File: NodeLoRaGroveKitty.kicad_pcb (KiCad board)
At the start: 2 copper layers, 37 parts, among them P1 PICKIT PROGRAMMER, P2 Battery, P3 A0, P4 D9, P5 USB-Serial, P6 I2C, SW1 SW_PUSH, SW2 SW_PUSH, U1 AP2112, U2 MCP73831T-2ATI/OT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

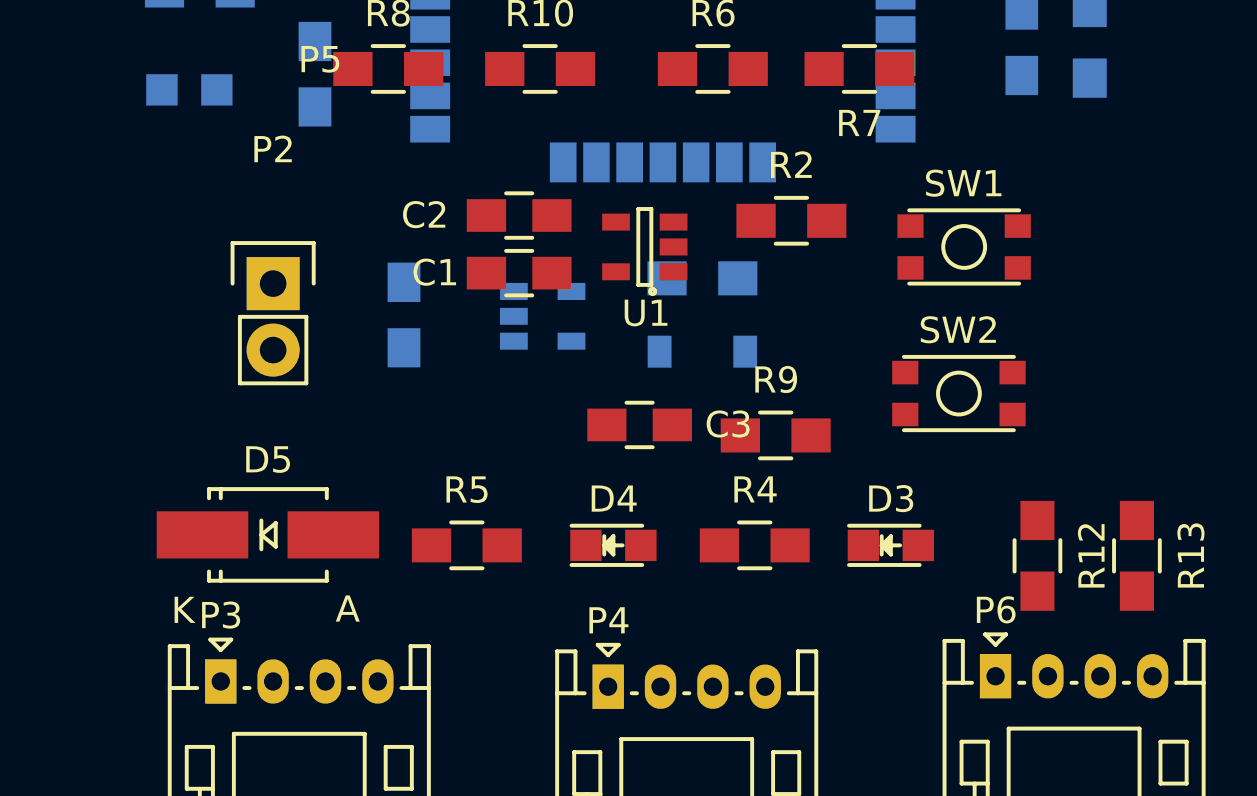
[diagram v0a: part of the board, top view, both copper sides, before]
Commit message: Validate footprints
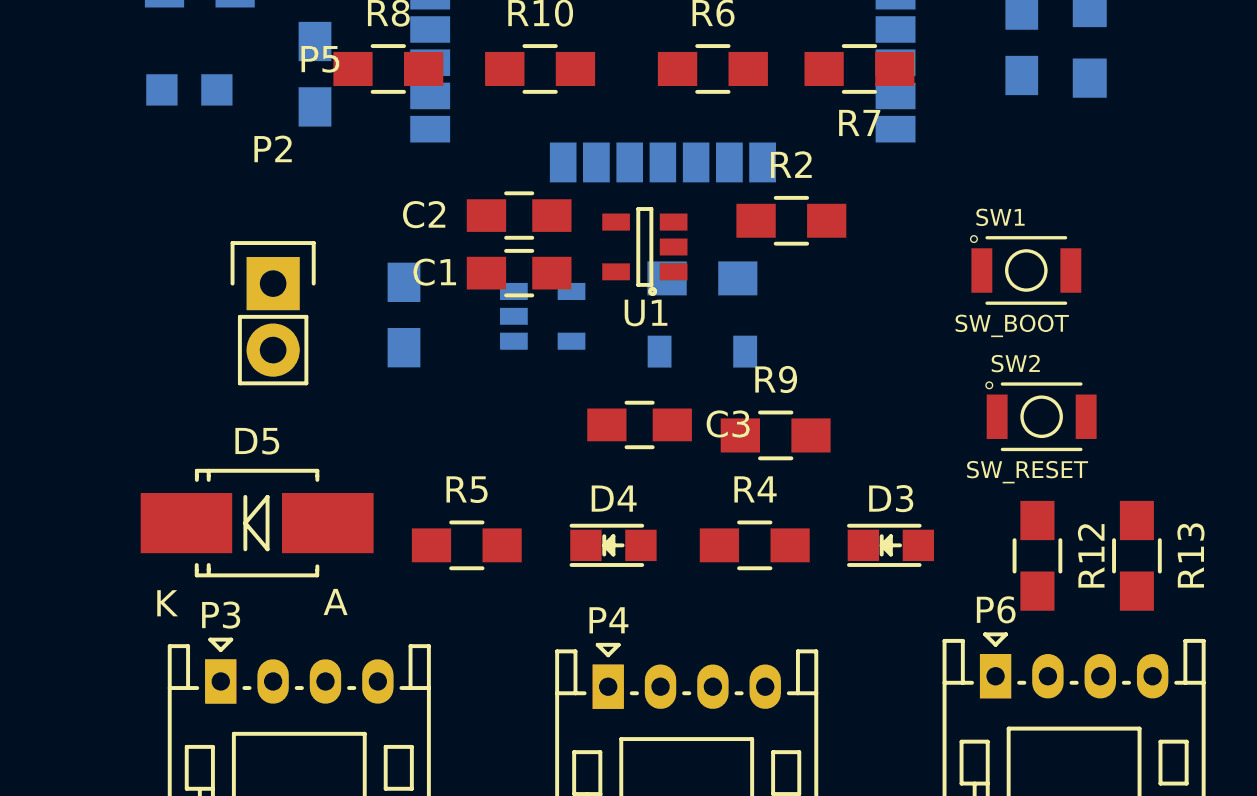
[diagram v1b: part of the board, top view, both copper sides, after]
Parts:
- D5: footprint Diodes_SMD:SMA_Handsoldering -> Diodes_SMD:SMB_Handsoldering
- SW1: value SW_PUSH -> SW_BOOT; footprint TIH:SW_SPST_KMR2 -> TIH:SW_B3U-1000P
- SW2: value SW_PUSH -> SW_RESET; footprint TIH:SW_SPST_KMR2 -> TIH:SW_B3U-1000P
- moved SW2 3.28 mm to (137.2, 129.3)
- moved SW1 2.54 mm to (136.6, 123.7)
- moved D5 0.61 mm to (107.2, 133.3)
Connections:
- P3 pad 2: +3V3 -> VCC
- P4 pad 2: +3V3 -> VCC
- P6 pad 2: +3V3 -> VCC

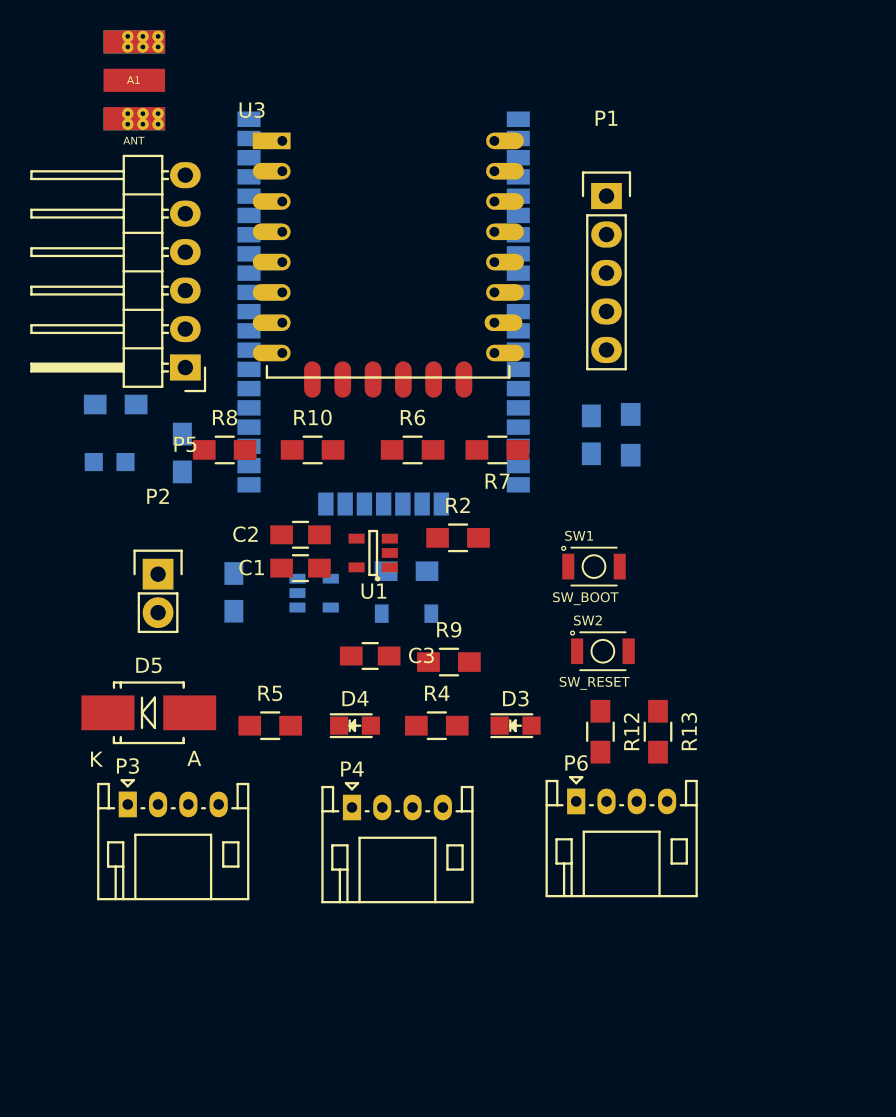
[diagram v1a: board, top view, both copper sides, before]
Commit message: Add first PCB design
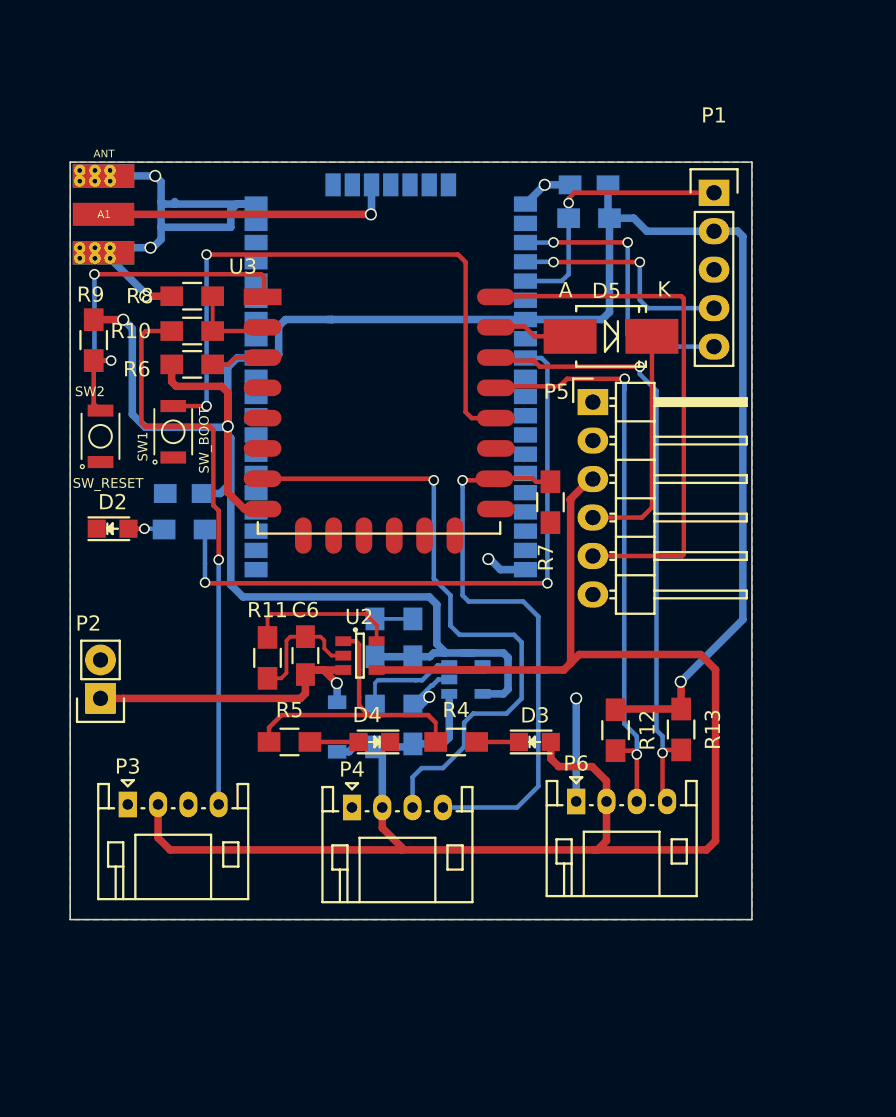
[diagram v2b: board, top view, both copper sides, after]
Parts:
- C1, C2, C3, R2, U1: moved to B.Cu
- C6, D2, R11, U2: moved to F.Cu
- moved D5 39.4 mm to (137.7, 108.5), turned to 180 degrees
- moved MODULE1 37.1 mm to (132.1, 125.2), turned to 180 degrees
- moved SW2 36.1 mm to (104.0, 115.1), turned to 90 degrees
- moved R9 31.6 mm to (103.5, 108.8), turned to 270 degrees
- moved SW1 29.2 mm to (108.8, 114.8), turned to 90 degrees
- moved P5 27.0 mm to (136.5, 112.8), turned to 0 degrees
- moved C5 16.5 mm to (136.2, 98.5), turned to 180 degrees
- moved R6 15.6 mm to (110.0, 110.3)
- moved R3 14.6 mm to (136.2, 100.7), turned to 180 degrees
- moved R2 13.6 mm to (122.1, 134.2), turned to 270 degrees
- moved C1 12.7 mm to (124.6, 134.2), turned to 90 degrees
- moved R10 11.2 mm to (110.0, 108.2)
- moved R11 10.8 mm to (115.0, 129.7), turned to 270 degrees
- moved R8 10.4 mm to (110.0, 105.8), turned to 180 degrees
- moved U1 10.4 mm to (128.1, 131.2), turned to 0 degrees
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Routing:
- net +3V3: track 0.00 -> 165.3 mm, vias 0 -> 3
- net VCC: track 0.00 -> 128.5 mm
- net GND: track 0.00 -> 58.2 mm, vias 0 -> 7
- net Net-(MODULE1-Pad36): track 0.00 -> 42.2 mm, vias 0 -> 2
- net /GPIO13: track 0.00 -> 42.1 mm, vias 0 -> 1
- net /SCL: track 0.00 -> 41.7 mm, vias 0 -> 2
- net /GPIO0: track 0.00 -> 40.9 mm, vias 0 -> 2
- net /SDA: track 0.00 -> 39.6 mm, vias 0 -> 2
- net /A0: track 0.00 -> 37.7 mm, vias 0 -> 1
- net /GPIO15: track 0.00 -> 36.8 mm, vias 0 -> 1
- net /TX: track 0.00 -> 35.7 mm
- net /RST: track 0.00 -> 24.3 mm, vias 0 -> 2
- net +BATT: track 0.00 -> 20.4 mm, vias 0 -> 1
- net Net-(R4-Pad1): track 0.00 -> 20.0 mm
- net Net-(A1-Pad1): track 0.00 -> 19.6 mm, vias 0 -> 1
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- added copper zone on B.Cu, net GND
- added copper zone on F.Cu, net GND
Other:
- board outline added: 45 x 50 mm
- net class Default: trace_width 0.25 -> 0.3; via_dia 0.6 -> 0.7; via_drill 0.4 -> 0.5
- net class vcc added: clearance 0.2, trace_width 0.5, via_dia 0.8, via_drill 0.6

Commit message: Added Logos
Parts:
- added G***: LOGO, TIH:electronic_cats_logo_4x3, F.Cu at (131.1, 129.3)
- added REF***: OSHW-Logo2_7.3x6mm_SilkScreen, Symbols:OSHW-Logo2_7.3x6mm_SilkScreen, B.Cu at (133.6, 131.1)
- added REF***: FCC-Logo_7.3x6mm_SilkScreen, Symbols:FCC-Logo_7.3x6mm_SilkScreen, B.Cu at (113.3, 131.3)
- renumbered MODULE1 to RN2903
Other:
- board text added: "LoRaCat: Kitty"

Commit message: Added labels pinout
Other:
- board text added: "GND VCC D13 D15"
- board text added: "GND VCC NC A0"
- board text added: "GND VCC SDA SCL"
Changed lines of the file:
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@@
     (area 101.949999 96.949999 147.050001 147.050001)
     (thickness 1.6)
-    (drawings 7)
+    (drawings 10)
     (tracks 368)
     (zones 0)
@@
       (xy 1.463092 -2.5146) (xy 1.492024 -2.514153)) (layer F.SilkS) (width 0.01))
   )
+  (gr_text "GND\nVCC\nSDA\nSCL" (at 138.684 142.748 90) (layer B.SilkS)
+    (effects (font (size 1.5 1.5) (thickness 0.3)) (justify mirror))
+  )
+  (gr_text "GND\nVCC\nD13\nD15" (at 123.952 143.256 90) (layer B.SilkS)
+    (effects (font (size 1.5 1.5) (thickness 0.3)) (justify mirror))
+  )
+  (gr_text "GND\nVCC\nNC\nA0" (at 108.966 142.748 90) (layer B.SilkS)
+    (effects (font (size 1.5 1.5) (thickness 0.3)) (justify mirror))
+  )
   (gr_text "LoRaCat:\nKitty" (at 109.728 131.064) (layer F.SilkS)

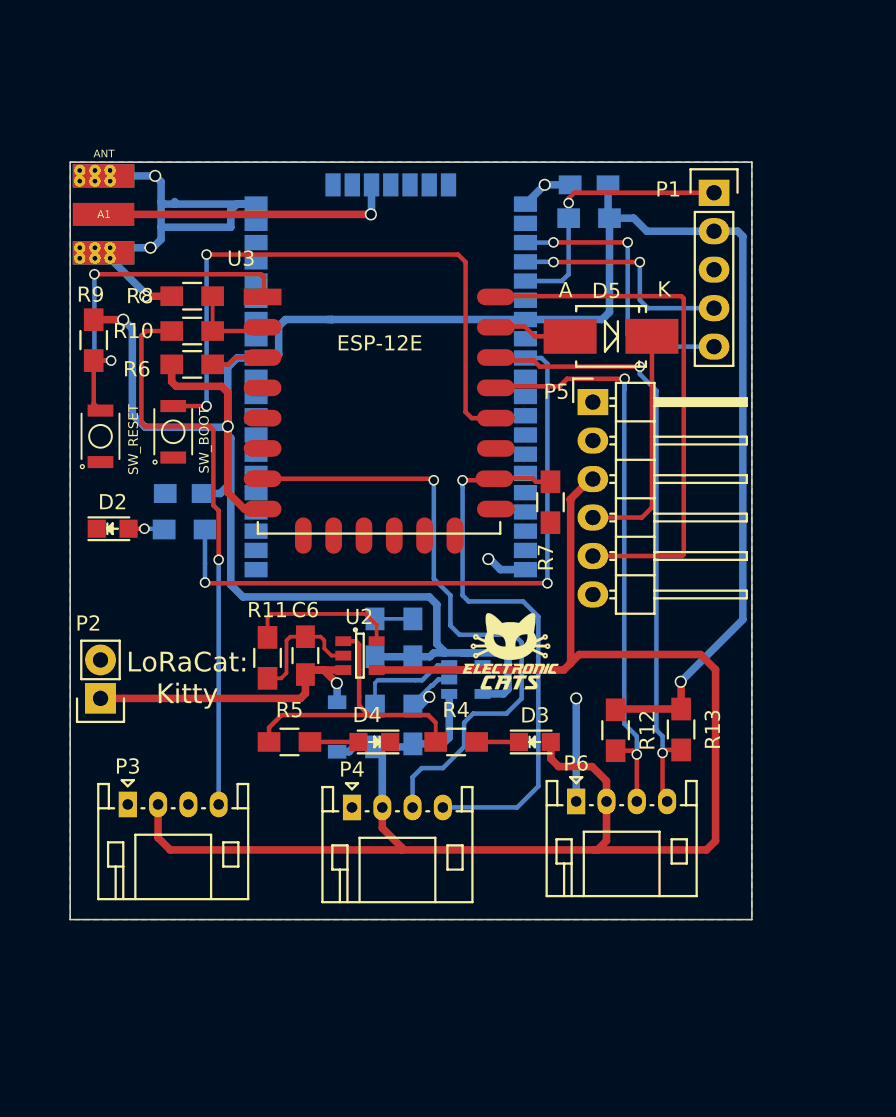
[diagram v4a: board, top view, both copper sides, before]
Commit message: Fix non-copper area
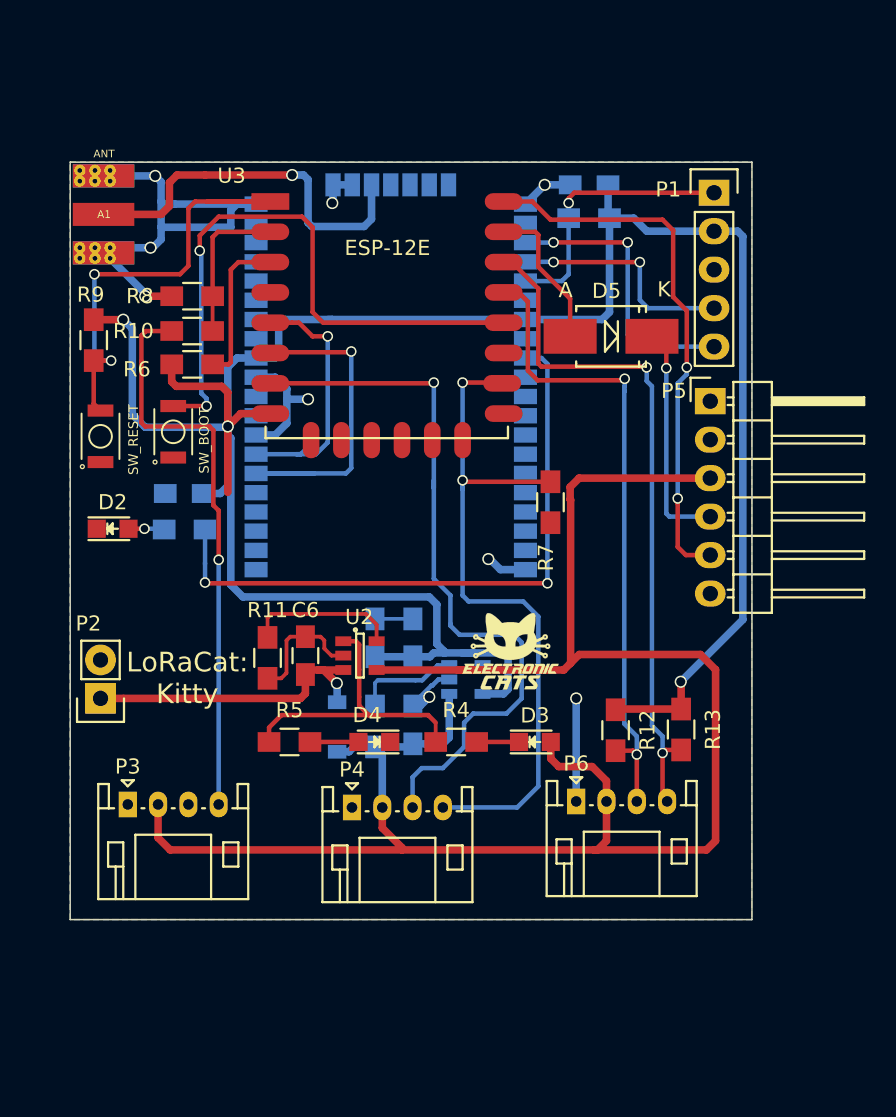
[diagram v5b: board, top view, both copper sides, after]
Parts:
- moved P5 7.75 mm to (144.2, 112.8)
- moved U3 6.32 mm to (115.9, 99.6)
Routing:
- net /S_RX/GPIO12: track 0.00 -> 22.6 mm, vias 0 -> 1
- net /S_TX/GPIO14: track 0.00 -> 16.2 mm, vias 0 -> 1
- net GND: track 58.2 -> 68.8 mm, vias 7 -> 9
- net /GPIO15: track 36.8 -> 46.2 mm, vias 1 -> 2
- net /RST: track 24.3 -> 32.5 mm
- net VCC: track 128.5 -> 136.8 mm
- net /CH_PD: track 4.19 -> 10.9 mm
- net /GPIO13: track 42.1 -> 48.5 mm
- net Net-(A1-Pad1): track 19.6 -> 25.2 mm
- net /RX: track 5.16 -> 10.6 mm
- net /SCL: track 41.7 -> 47.0 mm
- net /ADC: track 6.40 -> 10.9 mm
- net /SDA: track 39.6 -> 43.7 mm
- net /GPIO0: track 40.9 -> 39.7 mm
- net /TX: track 35.7 -> 36.6 mm, vias 0 -> 2
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
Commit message: Fix label's
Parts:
- moved SW2 0.30 mm to (104.0, 114.8)
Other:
- board text added: "+Batt"
- board text added: "CTS"
- board text added: "DTR"
- board text added: "GND"
- board text added: "RX"
- board text added: "TX"
- board text added: "Vcc"
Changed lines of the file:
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@@
   (general
     (links 107)
-    (no_connects 2)
+    (no_connects 1)
     (area 101.949999 96.949999 147.050001 147.050001)
     (thickness 1.6)
-    (drawings 10)
+    (drawings 18)
     (tracks 443)
     (zones 0)
@@
   )
   (layers
-    (0 F.Cu signal)
-    (31 B.Cu signal)
+    (0 F.Cu signal hide)
+    (31 B.Cu signal hide)
     (32 B.Adhes user)
     (33 F.Adhes user)
@@
     (descr "Through hole pin header")
     (tags "pin header")
-    (fp_text reference P5 (at -2.4 -0.68) (layer F.SilkS)
+    (fp_text reference P5 (at 1.7 15.17) (layer F.SilkS)
       (effects (font (size 1 1) (thickness 0.15)))
     )
@@
   )
   (module TIH:SW_B3U-1000P (layer F.Cu)
-    (at 104 115.1 90)
+    (at 104 114.8 90)
     (solder_mask_margin 0.1)
     (attr smd)
@@
       (xy 1.463092 -2.5146) (xy 1.492024 -2.514153)) (layer F.SilkS) (width 0.01))
   )
+  (gr_text GND (at 108 129.8) (layer F.SilkS)
+    (effects (font (size 1.5 1.5) (thickness 0.3)))
+  )
+  (gr_text "+Batt\n" (at 108.95 132.45) (layer F.SilkS)
+    (effects (font (size 1.5 1.5) (thickness 0.3)))
+  )
+  (gr_text DTR (at 140.6 125.7) (layer F.SilkS)
+    (effects (font (size 1.5 1.5) (thickness 0.3)))
+  )
+  (gr_text CTS (at 140.5 115.5) (layer F.SilkS)
+    (effects (font (size 1.5 1.5) (thickness 0.3)))
+  )
+  (gr_text Vcc (at 140.7 117.75) (layer F.SilkS)
+    (effects (font (size 1.5 1.5) (thickness 0.3)))
+  )
+  (gr_text RX (at 141.05 120.6) (layer F.SilkS)
+    (effects (font (size 1.5 1.5) (thickness 0.3)))
+  )
+  (gr_text "TX\n" (at 141.35 123.05) (layer F.SilkS)
+    (effects (font (size 1.5 1.5) (thickness 0.3)))
+  )
+  (gr_text GND (at 140.5 112.85) (layer F.SilkS)
+    (effects (font (size 1.5 1.5) (thickness 0.3)))
+  )
   (gr_text "GND\nVCC\nSDA\nSCL" (at 138.684 142.748 90) (layer B.SilkS)
     (effects (font (size 1.5 1.5) (thickness 0.3)) (justify mirror))
@@
     (effects (font (size 1.5 1.5) (thickness 0.3)) (justify mirror))
   )
-  (gr_text "LoRaCat:\nKitty" (at 109.728 131.064) (layer F.SilkS)
+  (gr_text "LoRaCat: Kitty" (at 122.15 120.2) (layer F.SilkS)
     (effects (font (size 1.3 1.3) (thickness 0.25)))
   )
@@
   (segment (start 111.75 101.6) (end 115.91 101.6) (width 0.3) (layer F.Cu) (net 47))
   (segment (start 111.4 105.85) (end 111.4 108.15) (width 0.25) (layer F.Cu) (net 47))
+  (segment (start 103.55 110.1) (end 103.55 112.65) (width 0.3) (layer F.Cu) (net 48))
+  (segment (start 103.55 112.65) (end 104 113.1) (width 0.3) (layer F.Cu) (net 48))
   (segment (start 109.8 103.85) (end 109.25 104.4) (width 0.3) (layer F.Cu) (net 48))
   (segment (start 109.25 104.4) (end 103.6 104.4) (width 0.3) (layer F.Cu) (net 48))
@@
   (segment (start 103.6 104.4) (end 103.6 109.6) (width 0.3) (layer B.Cu) (net 48))
   (via (at 103.6 104.4) (size 0.7) (drill 0.5) (layers F.Cu B.Cu) (net 48))
-  (segment (start 103.55 110.1) (end 103.55 112.95) (width 0.3) (layer F.Cu) (net 48))
-  (segment (start 103.55 112.95) (end 104 113.4) (width 0.3) (layer F.Cu) (net 48))
   (segment (start 115.025 127.075) (end 115.025 128.375) (width 0.25) (layer F.Cu) (net 49))
   (segment (start 115.275 126.825) (end 115.025 127.075) (width 0.25) (layer F.Cu) (net 49))
